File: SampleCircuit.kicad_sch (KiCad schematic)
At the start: 50 parts, among them J1 24V INPUT, J2 12V TEST, J3 5V TEST, J4 3.3V TEST, J5 SPEAKER, SW1 RESET, SW2 BOOT, U1 LMZM23601SILR, U15 TLV803S, U2 ESP32-S3-WROOM-1, U23 RV-3028-C7, U24 LMZM23601SILR, U25 LMZM23601SILR, U5 NS4168, U6 MicroSD

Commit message: Fix LMZM23601 PSU issues #2 and #3: add U24 input cap, upgrade U1 output cap
- Add C108 (10uF 35V GRM32ER7YA106KA12L, C97973) as second input cap for
  U24 (3.3V converter), matching the dual-cap pattern on U1 and U25
- Upgrade C3 (U1 12V output cap) from 47uF 16V to 47uF 25V
  (GRM32EC81E476KE15L, C86211) for proper voltage derating on 12V rail

Co-Authored-By: Claude Opus 4.6 <noreply@anthropic.com>
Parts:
- removed B3: CR1220, JLCImport:CR2032-BS-2-1, symbol JLCImport:CR2032-BS-2-1
- removed C104, C2, C39, C5, C94: 100nF, JLCImport:CC0805KRX7R9BB104, symbol JLCImport:CC0805KRX7R9BB104
- removed C105: 10uF, JLCImport:CL21A106KAYNNNE, symbol JLCImport:CL21A106KAYNNNE
- removed C106: 10uF 35V, JLCImport:GRM32ER7YA106KA12L, symbol JLCImport:GRM32ER7YA106KA12L
- removed C107: 680uF 35V, JLCImport:EEEFT1V681UP, symbol JLCImport:EEEFT1V681UP
- removed C4: 1uF, JLCImport:CL21B105KBFNNNE, symbol JLCImport:CL21B105KBFNNNE
- removed C93: 10uF, JLCImport:GRM32ER7YA106KA12L, symbol JLCImport:GRM32ER7YA106KA12L
- removed D10: SMBJ26CA, JLCImport:SMBJ26CA_C89651, symbol JLCImport:SMBJ26CA_C89651
- removed D9: SS34, JLCImport:SS34_C8678, symbol JLCImport:SS34_C8678
- removed R48, R89: 10k, JLCImport:0805W8F1002T5E, symbol JLCImport:0805W8F1002T5E
- removed R94: 1k, JLCImport:0805W8F1001T5E, symbol JLCImport:0805W8F1001T5E
- removed SW1: RESET, JLCImport:TS665WS_C2686403, symbol JLCImport:TS665WS_C2686403
- removed SW2: BOOT, JLCImport:TS665WS_C2686403, symbol JLCImport:TS665WS_C2686403
- removed U15: TLV803S, JLCImport:TLV803SDBZR, symbol JLCImport:TLV803SDBZR
- removed U23: RV-3028-C7, JLCImport:RV-3028-C7_32_768KHZ_1PPM_TA_QC, symbol JLCImport:RV-3028-C7_32_768KHZ_1PPM_TA_QC
- removed U24, U25: LMZM23601SILR, JLCImport:LMZM23601SILR, symbol JLCImport:LMZM23601SILR
- added C1, C15: 10uF, JLCImport:CL21A106KAYNNNE, symbol JLCImport:CL21A106KAYNNNE
- added C1: 1uF, JLCImport:CL21B105KBFNNNE, symbol JLCImport:CL21B105KBFNNNE
- added C11: 680uF 35V, JLCImport:EEEFT1V681UP, symbol JLCImport:EEEFT1V681UP
- added C16, C2 (x2): 100nF, JLCImport:CC0805KRX7R9BB104, symbol JLCImport:CC0805KRX7R9BB104
- added C2: 10uF 35V, JLCImport:GRM32ER7YA106KA12L, symbol JLCImport:GRM32ER7YA106KA12L
- added D1: SS34, JLCImport:SS34_C8678, symbol JLCImport:SS34_C8678
- added D2: SMBJ26CA, JLCImport:SMBJ26CA_C89651, symbol JLCImport:SMBJ26CA_C89651
- added R6: 1.0M, JLCImport:0805W8F1004T5E, symbol JLCImport:0805W8F1004T5E
- added R7: 100k, JLCImport:0805W8F1003T5E, symbol JLCImport:0805W8F1003T5E
- added U4: MAX98357A, JLCImport:MAX98357AETE_T, symbol JLCImport:MAX98357AETE_T
- added U5, U6: LMZM23601SILR, JLCImport:LMZM23601SILR, symbol JLCImport:LMZM23601SILR
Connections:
- net +12V: no longer J2.1, U1.6 (VOUT)
- net +24V: now also D1.1 (K); no longer J1.1
- net +3.3V: now also C1.1, C11.2, C3.1, C31.1, C32.1, C33.1, C34.1, C35.1, R2.2, R20.1, R32.2, R4.2, U6.6 (VSS), U6.8 (DAT1), U6.9 (SHIELD), C1.1, C1.2, C11.2, C15.2, C16.2, C2.1, C2.1, C2.1, C2.2, C2.2, D2.2 (A), R6.2, R7.1; no longer J4.1, Mem1.8 (VCC), U2.2 (3V3)
- net +5V: now also C15.1, C16.1, R6.1; no longer C17.1, C18.1, J3.1, R3.1, U5.6 (VDD)
- net AMP_EN: no longer U2.7 (IO7), U5.1 (CTRL)
- net CS_SD: no longer U2.11 (IO18)
- net DIN: now also R7.2; no longer U2.6 (IO6), U5.4 (SDATA)
- net OUTN: no longer J5.1, U5.5 (VON)
- net RX: no longer U2.36 (RXD0)
- net TX: no longer U2.37 (TXD0)
- net UD+: no longer U2.14 (IO20)
- net at R1.2, R2.1: no longer U1.7 (FB)
- net at C34.2, D8.1 (K): now also C11.1
- net BCLK: no longer names the net of U5.3 (BCLK)
- net BCLK: no longer U2.4 (IO4)
- net BOOT: no longer names the net of U2.27 (IO0)
- net CS_FLASH: no longer names the net of Mem1.2 (CD/SDD3)
- net CS_FLASH: no longer U2.12 (IO8)
- net Enable: no longer names the net of U2.3 (EN)
- removed net GND: C1.1, C11.2, C17.2, C18.2, C3.1, C31.1, C32.1, C33.1, C34.1, C35.1, J1.2, J2.2, J3.2, J4.2, Mem1.4 (VSS), R2.2, R20.1, R32.2, R4.2, U1.1 (GND), U1.11 (EP), U1.2 (MODE/SYNC), U2.1 (GND), U2.40 (GND), U2.41 (GND), U5.7 (GND), U5.9 (EP), U6.6 (VSS), U6.9 (SHIELD)
- net LRCLK: no longer names the net of U5.2 (LRCLK)
- net LRCLK: no longer U2.5 (IO5)
- net OUTP: no longer names the net of U5.8 (VOP)
- net OUTP: no longer J5.2
- net SCL: no longer names the net of U2.39 (IO1)
- net SDA: no longer names the net of U2.38 (IO2)
- removed net SD_CLK: Mem1.3 (SCLK), U2.10 (IO17), U6.5 (CLK)
- removed net SD_MISO: Mem1.6 (SDD0), U2.8 (IO15), U6.7 (DAT0)
- removed net SD_MOSI: Mem1.5 (CMD), U2.9 (IO16), U6.3 (CMD)
- net UD-: no longer names the net of U2.13 (IO19)
- new net: C1.2, C2.2, D1.2 (A), D2.1 (K)
- now unconnected: U1.3 (VIN), U1.4 (EN)
- no-connect marks 40 -> 43

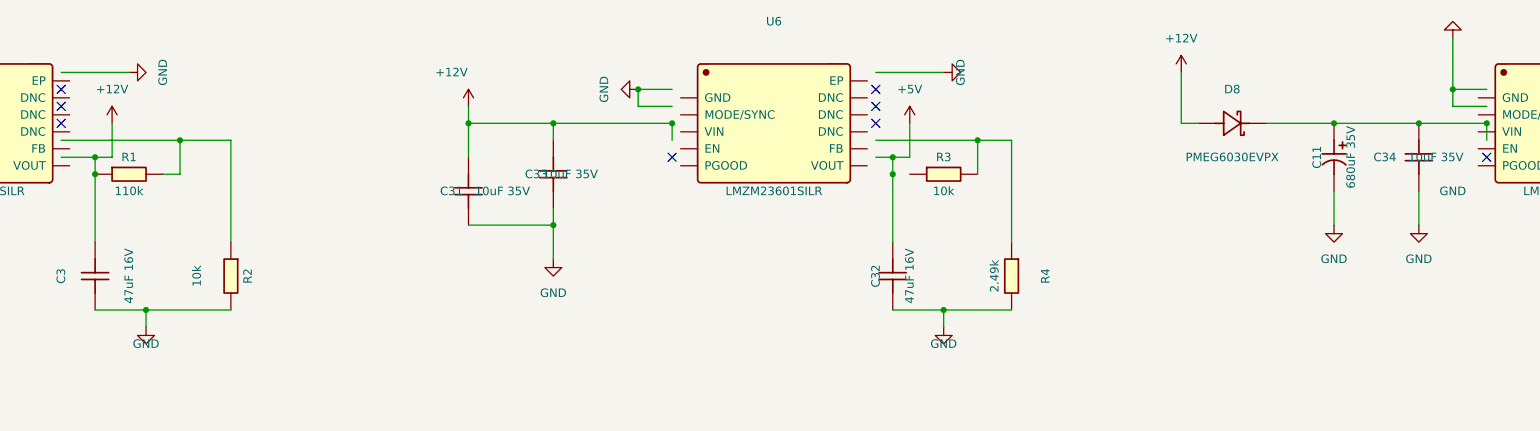
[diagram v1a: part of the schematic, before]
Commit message: Fix LMZM23601 PSU issues #2 and #3: add U24 input cap, upgrade U1 output cap
- Add C108 (10uF 35V GRM32ER7YA106KA12L, C97973) as second input cap for
  U24 (3.3V converter), matching the dual-cap pattern on U1 and U25
- Upgrade C3 (U1 12V output cap) from 47uF 16V to 47uF 25V
  (GRM32EC81E476KE15L, C86211) for proper voltage derating on 12V rail
- Add GRM32EC81E476KE15L lib_symbol (muRata 47uF 25V X5R 1210)

Co-Authored-By: Claude Opus 4.6 <noreply@anthropic.com>
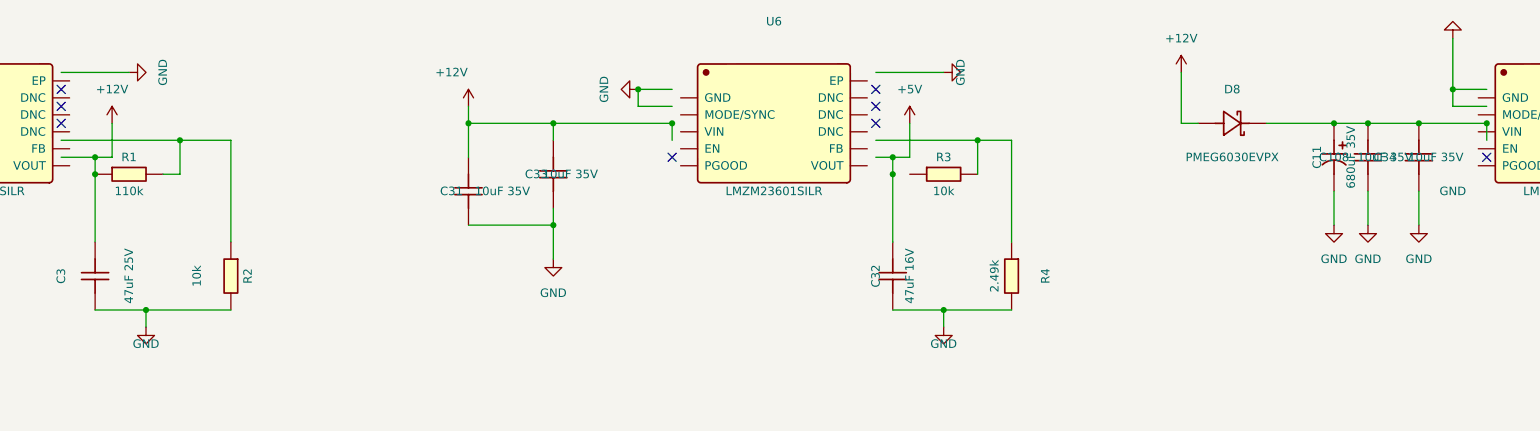
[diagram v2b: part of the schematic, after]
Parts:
- added C108: 10uF 35V, JLCImport:GRM32ER7YA106KA12L, symbol JLCImport:GRM32ER7YA106KA12L
- C3: value 47uF 16V -> 47uF 25V; footprint JLCImport:1206X476M160NT -> JLCImport:GRM32EC81C476KE15L; symbol JLCImport:1206X476M160NT -> JLCImport:GRM32EC81E476KE15L; LCSC C172351 -> C86211
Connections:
- net +3.3V: now also C108.1
- net at C11.1, C34.2, D8.1 (K): now also C108.2
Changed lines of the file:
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@@
   )
   (symbol
-    (lib_id "JLCImport:1206X476M160NT")
+    (lib_id "JLCImport:GRM32EC81E476KE15L")
     (at 167.64 124.46 270)
     (unit 1)
@@
       (effects (font (size 1.27 1.27)))
     )
-    (property "Value" "47uF 16V"
+    (property "Value" "47uF 25V"
       (at 172.72 124.46 0)
       (effects (font (size 1.27 1.27)))
     )
-    (property "Footprint" "JLCImport:1206X476M160NT"
+    (property "Footprint" "JLCImport:GRM32EC81C476KE15L"
       (at 167.64 124.46 0)
       (effects (font (size 1.27 1.27)) hide)
     )
-    (property "LCSC" "C172351"
+    (property "LCSC" "C86211"
       (at 167.64 124.46 0)
       (effects (font (size 1.27 1.27)) hide)
@@
           (unit 1)
         )
+      )
+    )
+  )
+  (junction (at 358.14 101.6)
+    (diameter 0)
+    (color 0 0 0 0)
+  )
+  (wire (pts (xy 358.14 111.76) (xy 358.14 116.84))
+    (stroke (width 0) (type default))
+  )
+  (symbol
+    (lib_id "JLCImport:GRM32ER7YA106KA12L")
+    (at 358.14 106.68 0)
+    (unit 1)
+    (exclude_from_sim no)
+    (in_bom yes)
+    (on_board yes)
+    (dnp no)
+    (property "Reference" "C108"
+      (at 353.06 106.68 0)
+      (effects (font (size 1.27 1.27)))
+    )
+    (property "Value" "10uF 35V"
+      (at 360.68 106.68 0)
+      (effects (font (size 1.27 1.27)))
+    )
+    (property "Footprint" "JLCImport:GRM32ER7YA106KA12L"
+      (at 358.14 106.68 0)
+      (effects (font (size 1.27 1.27)) hide)
+    )
+    (property "LCSC" "C97973"
+      (at 358.14 106.68 0)
+      (effects (font (size 1.27 1.27)) hide)
+    )
+    (instances
+      (project "SampleCircuit"
+        (path "/f1a2b3c4-d5e6-7f89-0a1b-c2d3e4f5a6b7"
+          (reference "C108")
+          (unit 1)
+        )
+      )
+    )
+  )
+  (symbol
+    (lib_id "power:GND")
+    (at 358.14 116.84 0)
+    (unit 1)
+    (exclude_from_sim no)
+    (in_bom yes)
+    (on_board yes)
+    (dnp no)
+    (property "Reference" "#PWR105"
+      (at 358.14 121.92 0)
+      (effects (font (size 1.27 1.27)) hide)
+    )
+    (property "Value" "GND"
+      (at 358.14 121.92 0)
+      (effects (font (size 1.27 1.27)))
+    )
+    (property "Footprint" ""
+      (at 358.14 116.84 0)
+      (effects (font (size 1.27 1.27)) hide)
+    )
+    (instances
+      (project "SampleCircuit"
+        (path "/f1a2b3c4-d5e6-7f89-0a1b-c2d3e4f5a6b7"
+          (reference "#PWR105")
+          (unit 1)
+        )

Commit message: Add I2C pullup resistors and apply PSU audit fixes
- R33/R34: 4.22k pullups on SCL/SDA to +3.3V near ESP32
- Fix #2: C108 10uF 35V input cap for U24 3.3V converter
- Fix #3: C3 upgraded from 47uF 16V to 47uF 25V on U1 output
Applied via kicad-patch-tools (non-destructive patching)

Co-Authored-By: Claude Opus 4.6 <noreply@anthropic.com>
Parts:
- removed C1, C15: 10uF, JLCImport:CL21A106KAYNNNE, symbol JLCImport:CL21A106KAYNNNE
- removed C1: 1uF, JLCImport:CL21B105KBFNNNE, symbol JLCImport:CL21B105KBFNNNE
- removed C11: 680uF 35V, JLCImport:EEEFT1V681UP, symbol JLCImport:EEEFT1V681UP
- removed C16, C2 (x2): 100nF, JLCImport:CC0805KRX7R9BB104, symbol JLCImport:CC0805KRX7R9BB104
- removed C2: 10uF 35V, JLCImport:GRM32ER7YA106KA12L, symbol JLCImport:GRM32ER7YA106KA12L
- removed C3: 47uF 25V, JLCImport:GRM32EC81C476KE15L, symbol JLCImport:GRM32EC81E476KE15L
- removed D1: SS34, JLCImport:SS34_C8678, symbol JLCImport:SS34_C8678
- removed D2: SMBJ26CA, JLCImport:SMBJ26CA_C89651, symbol JLCImport:SMBJ26CA_C89651
- removed R6: 1.0M, JLCImport:0805W8F1004T5E, symbol JLCImport:0805W8F1004T5E
- removed R7: 100k, JLCImport:0805W8F1003T5E, symbol JLCImport:0805W8F1003T5E
- removed U4: MAX98357A, JLCImport:MAX98357AETE_T, symbol JLCImport:MAX98357AETE_T
- removed U5, U6: LMZM23601SILR, JLCImport:LMZM23601SILR, symbol JLCImport:LMZM23601SILR
- added B3: CR1220, JLCImport:CR2032-BS-2-1, symbol JLCImport:CR2032-BS-2-1
- added C104, C2, C39, C5, C94: 100nF, JLCImport:CC0805KRX7R9BB104, symbol JLCImport:CC0805KRX7R9BB104
- added C105: 10uF, JLCImport:CL21A106KAYNNNE, symbol JLCImport:CL21A106KAYNNNE
- added C106: 10uF 35V, JLCImport:GRM32ER7YA106KA12L, symbol JLCImport:GRM32ER7YA106KA12L
- added C107: 680uF 35V, JLCImport:EEEFT1V681UP, symbol JLCImport:EEEFT1V681UP
- added C3: 47uF 25V, JLCImport:GRM32EC81C476KE15L, symbol JLCImport:GRM32EC81C476KE15L
- added C4: 1uF, JLCImport:CL21B105KBFNNNE, symbol JLCImport:CL21B105KBFNNNE
- added C93: 10uF, JLCImport:GRM32ER7YA106KA12L, symbol JLCImport:GRM32ER7YA106KA12L
- added R33, R34: 4.22k, JLCImport:0805W8F4221T5E, symbol JLCImport:0805W8F4221T5E
- added R48, R89: 10k, JLCImport:0805W8F1002T5E, symbol JLCImport:0805W8F1002T5E
- added R94: 1k, JLCImport:0805W8F1001T5E, symbol JLCImport:0805W8F1001T5E
- added SW1: RESET, JLCImport:TS665WS_C2686403, symbol JLCImport:TS665WS_C2686403
- added SW2: BOOT, JLCImport:TS665WS_C2686403, symbol JLCImport:TS665WS_C2686403
- added U15: TLV803S, JLCImport:TLV803SDBZR, symbol JLCImport:TLV803SDBZR
- added U23: RV-3028-C7, JLCImport:RV-3028-C7_32_768KHZ_1PPM_TA_QC, symbol JLCImport:RV-3028-C7_32_768KHZ_1PPM_TA_QC
- added U24, U25: LMZM23601SILR, JLCImport:LMZM23601SILR, symbol JLCImport:LMZM23601SILR
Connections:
- net +12V: now also J2.1, U1.6 (VOUT), C3.2, U25.3 (VIN), U25.4 (EN)
- net +24V: now also C1.2, J1.1, U1.3 (VIN), U1.4 (EN), C106.2
- net +3.3V: now also J4.1, Mem1.8 (VCC), U2.2 (3V3), C105.1, C2.1, C39.1, C4.1, C5.1, C93.1, R33.2, R34.2, R48.1, U15.3 (VDD), U23.7 (VDD), U24.6 (VOUT); no longer C1.1, C108.1, C11.2, C31.1, C32.1, C33.1, C34.1, C35.1, R2.2, R20.1, R32.2, R4.2, U6.6 (VSS), U6.8 (DAT1), U6.9 (SHIELD)
- net +5V: now also C17.1, C18.1, J3.1, R3.1, U5.6 (VDD), U25.6 (VOUT)
- net AMP_EN: now also U2.7 (IO7), U5.1 (CTRL)
- net CS_SD: now also U2.11 (IO18)
- net DIN: now also U2.6 (IO6), U5.4 (SDATA)
- net OUTN: now also J5.1, U5.5 (VON)
- net RX: now also U2.36 (RXD0)
- net TX: now also U2.37 (TXD0)
- net UD+: now also U2.14 (IO20)
- net GND: now reaches J4.2
- net GND: now also C1.1, C108.1, C11.2, C17.2, C18.2, C31.1, C32.1, C33.1, C34.1, C35.1, J1.2, J2.2, J3.2, Mem1.4 (VSS), R2.2, R20.1, R32.2, R4.2, U1.1 (GND), U1.11 (EP), U1.2 (MODE/SYNC), U2.1 (GND), U2.40 (GND), U2.41 (GND), U5.7 (GND), U5.9 (EP), U6.6 (VSS), U6.9 (SHIELD), B3.2, C104.1, C105.2, C106.1, C107.2, C2.2, C3.1, C39.2, C4.2, C5.2, C93.2, C94.2, R89.2, SW1.2, SW2.2, U15.1 (GND), U23.5 (VSS), U24.1 (GND), U24.11 (EP), U24.2 (MODE/SYNC), U25.1 (GND), U25.11 (EP), U25.2 (MODE/SYNC)
- net at C108.2, C34.2, D8.1 (K): now also C107.1, U24.3 (VIN), U24.4 (EN)
- net CS_FLASH: now reaches Mem1.2 (CD/SDD3)
- net CS_FLASH: now also U2.12 (IO8)
- net SD_CLK: now reaches Mem1.3 (SCLK)
- net SD_CLK: now also U2.10 (IO17), U6.5 (CLK)
- net SD_MOSI: now reaches Mem1.5 (CMD)
- net SD_MOSI: now also U2.9 (IO16), U6.3 (CMD)
- net SD_MISO: now reaches Mem1.6 (SDD0)
- net SD_MISO: now also U2.8 (IO15), U6.7 (DAT0)
- net LRCLK: now reaches U5.2 (LRCLK)
- net LRCLK: now also U2.5 (IO5)
- net BCLK: now reaches U5.3 (BCLK)
- net BCLK: now also U2.4 (IO4)
- net OUTP: now reaches U5.8 (VOP)
- net OUTP: now also J5.2
- net UD-: now reaches U2.13 (IO19)
- net BOOT: now reaches U2.27 (IO0)
- net BOOT: now also SW2.1
- net Enable: now reaches U2.3 (EN)
- net Enable: now also C94.1, R48.2, SW1.1, U15.2 (RESET#)
- net SDA: now reaches U2.38 (IO2)
- net SDA: now also R34.1, U23.4 (SDA)
- net SCL: now reaches U2.39 (IO1)
- net SCL: now also R33.1, U23.3 (SCL)
- net at U1.7 (FB): now also R1.2, R2.1
- net at R3.2, R4.1: now also U25.7 (FB)
- net at R31.2, R32.1: now also U24.7 (FB)
- new net: B3.1, R94.2
- new net: R89.1, U23.8 (EVI)
- new net: C104.2, R94.1, U23.6 (VBACKUP)
- no-connect marks 43 -> 40
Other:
- moved on the sheet: C108

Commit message: Upgrade I2C pullups from 4.22k to 4.7k (R33, R34)
LCSC updated to C17673 (UNI-ROYAL 0805W8F4701T5E).
Applied via kicad-patch-tools.

Co-Authored-By: Claude Opus 4.6 <noreply@anthropic.com>
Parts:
- R33, R34: value 4.22k -> 4.7k; LCSC C17665 -> C17673
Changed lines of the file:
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@@
-	)
-	(symbol
-		(lib_id "JLCImport:0805W8F4221T5E")
-		(at 137.16 125.73 90)
-		(unit 1)
-		(exclude_from_sim no)
-		(in_bom yes)
-		(on_board yes)
-		(dnp no)
-		(property "Reference" "R33"
-			(at 140.716 126.492 90)
-			(effects
-				(font
-					(size 1.27 1.27)
-				)
-			)
-		)
-		(property "Value" "4.22k"
-			(at 140.716 128.778 90)
-			(effects
-				(font
-					(size 1.27 1.27)
-				)
-			)
-		)
-		(property "Footprint" "JLCImport:0805W8F4221T5E"
-			(at 137.16 125.73 0)
-			(effects
-				(font
-					(size 1.27 1.27)
-				)
-				(hide yes)
-			)
-		)
-		(property "Datasheet" ""
-			(at 137.16 125.73 0)
-			(effects
-				(font
-					(size 1.27 1.27)
-				)
-			)
-		)
-		(property "Description" ""
-			(at 137.16 125.73 0)
-			(effects
-				(font
-					(size 1.27 1.27)
-				)
-			)
-		)
-		(property "LCSC" "C17665"
-			(at 137.16 125.73 0)
-			(effects
-				(font
-					(size 1.27 1.27)
-				)
-				(hide yes)
-			)
-		)
-		(pin "1"
-		)
-		(pin "2"
-		)
-		(instances
-			(project "SampleCircuit"
-				(path "/f1a2b3c4-d5e6-7f89-0a1b-c2d3e4f5a6b7"
-					(reference "R33")
-					(unit 1)
-				)
-			)
-		)
-	)
-	(symbol
-		(lib_id "JLCImport:0805W8F4221T5E")
-		(at 127 125.73 90)
-		(unit 1)
-		(exclude_from_sim no)
-		(in_bom yes)
-		(on_board yes)
-		(dnp no)
-		(property "Reference" "R34"
-			(at 130.048 126.238 90)
-			(effects
-				(font
-					(size 1.27 1.27)
-				)
-			)
-		)
-		(property "Value" "4.22k"
-			(at 130.556 129.286 90)
-			(effects
-				(font
-					(size 1.27 1.27)
-				)
-			)
-		)
-		(property "Footprint" "JLCImport:0805W8F4221T5E"
-			(at 127 125.73 0)
-			(effects
-				(font
-					(size 1.27 1.27)
-				)
-				(hide yes)
-			)
-		)
-		(property "Datasheet" ""
-			(at 127 125.73 0)
-			(effects
-				(font
-					(size 1.27 1.27)
-				)
-			)
-		)
-		(property "Description" ""
-			(at 127 125.73 0)
-			(effects
-				(font
-					(size 1.27 1.27)
-				)
-			)
-		)
-		(property "LCSC" "C17665"
-			(at 127 125.73 0)
-			(effects
-				(font
-					(size 1.27 1.27)
-				)
-				(hide yes)
-			)
-		)
-		(pin "1"
-		)
-		(pin "2"
-		)
-		(instances
-			(project "SampleCircuit"
-				(path "/f1a2b3c4-d5e6-7f89-0a1b-c2d3e4f5a6b7"
-					(reference "R34")
-					(unit 1)
-				)
-			)
-		)
 	)
 	(symbol
@@
 		)
 	)
-	(sheet_instances
+  (symbol
+		(lib_id "JLCImport:0805W8F4221T5E")
+		(at 137.16 125.73 90)
+		(unit 1)
+		(exclude_from_sim no)
+		(in_bom yes)
+		(on_board yes)
+		(dnp no)
+		(property "Reference" "R33"
+			(at 140.716 126.492 90)
+			(effects
+				(font
+					(size 1.27 1.27)
+				)
+			)
+		)
+		(property "Value" "4.7k"
+			(at 140.716 128.778 90)
+			(effects
+				(font
+					(size 1.27 1.27)
+				)
+			)
+		)
+		(property "Footprint" "JLCImport:0805W8F4221T5E"
+			(at 137.16 125.73 0)
+			(effects
+				(font
+					(size 1.27 1.27)
+				)
+				(hide yes)
+			)
+		)
+		(property "Datasheet" ""
+			(at 137.16 125.73 0)
+			(effects
+				(font
+					(size 1.27 1.27)
+				)
+			)
+		)
+		(property "Description" ""
+			(at 137.16 125.73 0)
+			(effects
+				(font
+					(size 1.27 1.27)
+				)
+			)
+		)
+		(property "LCSC" "C17673"
+			(at 137.16 125.73 0)
+			(effects
+				(font
+					(size 1.27 1.27)
+				)
+				(hide yes)
+			)
+		)
+		(pin "1"
+		)
+		(pin "2"
+		)
+		(instances
+			(project "SampleCircuit"
+				(path "/f1a2b3c4-d5e6-7f89-0a1b-c2d3e4f5a6b7"
+					(reference "R33")
+					(unit 1)
+				)
+			)
+		)
+	)
+  (symbol
+		(lib_id "JLCImport:0805W8F4221T5E")
+		(at 127 125.73 90)
+		(unit 1)
+		(exclude_from_sim no)
+		(in_bom yes)
+		(on_board yes)
+		(dnp no)
+		(property "Reference" "R34"
+			(at 130.048 126.238 90)
+			(effects
+				(font
+					(size 1.27 1.27)
+				)
+			)
+		)
+		(property "Value" "4.7k"
+			(at 130.556 129.286 90)
+			(effects
+				(font
+					(size 1.27 1.27)
+				)
+			)
+		)
+		(property "Footprint" "JLCImport:0805W8F4221T5E"
+			(at 127 125.73 0)
+			(effects
+				(font
+					(size 1.27 1.27)
+				)
+				(hide yes)
+			)
+		)
+		(property "Datasheet" ""
+			(at 127 125.73 0)
+			(effects
+				(font
+					(size 1.27 1.27)
+				)
+			)
+		)
+		(property "Description" ""
+			(at 127 125.73 0)
+			(effects
+				(font
+					(size 1.27 1.27)
+				)
+			)
+		)
+		(property "LCSC" "C17673"
+			(at 127 125.73 0)
+			(effects
+				(font
+					(size 1.27 1.27)
+				)
+				(hide yes)
+			)
+		)
+		(pin "1"
+		)
+		(pin "2"
+		)
+		(instances
+			(project "SampleCircuit"
+				(path "/f1a2b3c4-d5e6-7f89-0a1b-c2d3e4f5a6b7"
+					(reference "R34")
+					(unit 1)
+				)
+			)
+		)
+	)	(sheet_instances
 		(path "/"
 			(page "1")

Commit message: Add 24V input protection: D9 (SS34 Schottky) + D10 (SMBJ26CA TVS)
D9: SS34 3A 40V series Schottky for reverse polarity protection
D10: SMBJ26CA 26V bidirectional TVS for transient suppression
Applied via kicad-patch-tools with add_lib_symbols support.

Co-Authored-By: Claude Opus 4.6 <noreply@anthropic.com>
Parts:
- added D10: SMBJ26CA, JLCImport:SMBJ26CA_C89651, symbol JLCImport:SMBJ26CA_C89651
- added D9: SS34, JLCImport:SS34_C8678, symbol JLCImport:SS34_C8678
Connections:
- net +24V: now also D9.1 (K); no longer C1.2, C106.2, U1.3 (VIN), U1.4 (EN)
- net GND: now also D10.2 (A)
- new net: C1.2, C106.2, D10.1 (K), D9.2 (A), U1.3 (VIN), U1.4 (EN)
